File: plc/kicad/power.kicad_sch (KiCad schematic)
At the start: 81 parts, among them Q5 BSS138LT1G, Q6 CSD19537Q3, SW3 TSD003B08026A03, U14 LMR16006XDDCR, U15 TPS54560BDDAR, U16 TPS26630RGER, U17 TPS7A5201QRGRRQ1

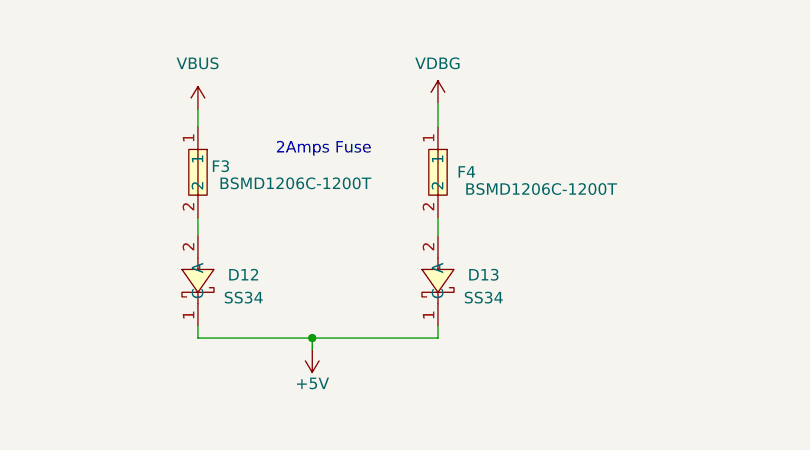
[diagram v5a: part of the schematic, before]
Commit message: Updated SMD fuses to fuse holders
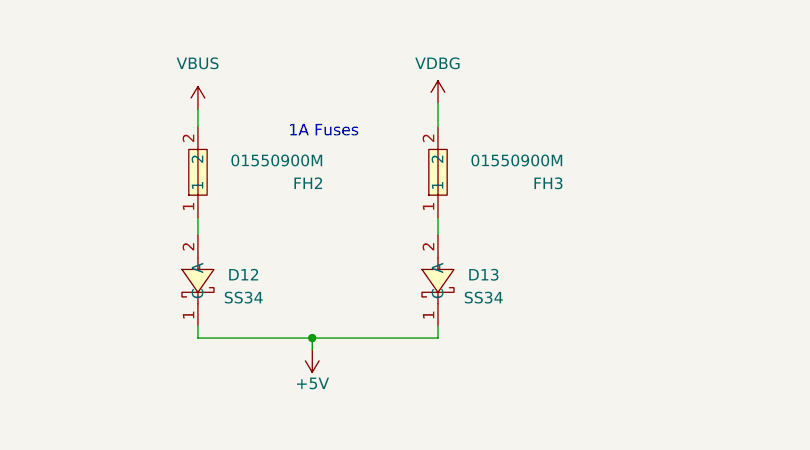
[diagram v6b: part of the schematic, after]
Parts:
- removed F3, F4: BSMD1206C-1200T, LibrePLC32:F1206, symbol LibrePLC32:BSMD1206C-1200T
- added FH2, FH3: 01550900M, LibrePLC32:FUSE-SMD_L9.8-W5.0_01550900M, symbol LibrePLC32:01550900M
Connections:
- net VBUS: now also FH2.2
- net VDBG: now also FH3.2
- net at D12.2 (A): now also FH2.1
- net at D13.2 (A): now also FH3.1
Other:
- note added: "1A Fuses"
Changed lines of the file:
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@@
 		)
 	)
-	(text "2Amps Fuse"
+	(text "1A Fuses"
 		(exclude_from_sim no)
-		(at 257.175 34.29 0)
+		(at 257.175 32.385 0)
 		(effects
 			(font
@@
 	)
 	(symbol
+		(lib_id "LibrePLC32:01550900M")
+		(at 243.205 36.83 90)
+		(unit 1)
+		(body_style 1)
+		(exclude_from_sim no)
+		(in_bom yes)
+		(on_board yes)
+		(in_pos_files yes)
+		(dnp no)
+		(property "Reference" "FH2"
+			(at 257.175 38.1 90)
+			(show_name no)
+			(do_not_autoplace no)
+			(effects
+				(font
+					(size 1.27 1.27)
+				)
+				(justify left)
+			)
+		)
+		(property "Value" "01550900M"
+			(at 257.175 35.56 90)
+			(show_name no)
+			(do_not_autoplace no)
+			(effects
+				(font
+					(size 1.27 1.27)
+				)
+				(justify left)
+			)
+		)
+		(property "Footprint" "LibrePLC32:FUSE-SMD_L9.8-W5.0_01550900M"
+			(at 250.825 36.83 0)
+			(hide yes)
+			(show_name no)
+			(do_not_autoplace no)
+			(effects
+				(font
+					(size 1.27 1.27)
+				)
+			)
+		)
+		(property "Datasheet" "https://lcsc.com/product-detail/Others_Littelfuse_01550900M_Littelfuse-01550900M_C108518.html"
+			(at 253.365 36.83 0)
+			(hide yes)
+			(show_name no)
+			(do_not_autoplace no)
+			(effects
+				(font
+					(size 1.27 1.27)
+				)
+			)
+		)
+		(property "Description" ""
+			(at 243.205 36.83 0)
+			(hide yes)
+			(show_name no)
+			(do_not_autoplace no)
+			(effects
+				(font
+					(size 1.27 1.27)
+				)
+			)
+		)
+		(property "Manufacturer" "Littelfuse(美国力特)"
+			(at 255.905 36.83 0)
+			(hide yes)
+			(show_name no)
+			(do_not_autoplace no)
+			(effects
+				(font
+					(size 1.27 1.27)
+				)
+			)
+		)
+		(property "MPN" "01550900M"
+			(at 258.445 36.83 0)
+			(hide yes)
+			(show_name no)
+			(do_not_autoplace no)
+			(effects
+				(font
+					(size 1.27 1.27)
+				)
+			)
+		)
+		(property "LCSC Part" "C108518"
+			(at 260.985 36.83 0)
+			(hide yes)
+			(show_name no)
+			(do_not_autoplace no)
+			(effects
+				(font
+					(size 1.27 1.27)
+				)
+			)
+		)
+		(pin "2"
+		)
+		(pin "1"
+		)
+		(instances
+			(project "LibrePLC32"
+				(path "/ef4c1a27-85a3-413a-9f93-a41c4f97eee5/7cb27fd0-1c73-4e87-ad2d-fb4e463ee9fb"
+					(reference "FH2")
+					(unit 1)
+				)
+			)
+		)
+	)
+	(symbol
 		(lib_id "Device:C")
 		(at 135.89 121.92 180)
@@
 	)
 	(symbol
-		(lib_id "LibrePLC32:BSMD1206C-1200T")
-		(at 243.205 36.83 270)
-		(unit 1)
-		(body_style 1)
-		(exclude_from_sim no)
-		(in_bom yes)
-		(on_board yes)
-		(in_pos_files yes)
-		(dnp no)
-		(property "Reference" "F3"
-			(at 245.745 36.195 90)
-			(show_name no)
-			(do_not_autoplace no)
-			(effects
-				(font
-					(size 1.27 1.27)
-				)
-			)
-		)
-		(property "Value" "BSMD1206C-1200T"
-			(at 254 38.1 90)
-			(show_name no)
-			(do_not_autoplace no)
-			(effects
-				(font
-					(size 1.27 1.27)
-				)
-			)
-		)
-		(property "Footprint" "LibrePLC32:F1206"
-			(at 235.585 36.83 0)
-			(hide yes)
-			(show_name no)
-			(do_not_autoplace no)
-			(effects
-				(font
-					(size 1.27 1.27)
-				)
-			)
-		)
-		(property "Datasheet" "https://www.lcsc.com/datasheet/C41367223.pdf"
-			(at 233.045 36.83 0)
-			(hide yes)
-			(show_name no)
-			(do_not_autoplace no)
-			(effects
-				(font
-					(size 1.27 1.27)
-				)
-			)
-		)
-		(property "Description" ""
-			(at 243.205 36.83 0)
-			(hide yes)
-			(show_name no)
-			(do_not_autoplace no)
-			(effects
-				(font
-					(size 1.27 1.27)
-				)
-			)
-		)
-		(property "Manufacturer" "BHFUSE(佰宏)"
-			(at 230.505 36.83 0)
-			(hide yes)
-			(show_name no)
-			(do_not_autoplace no)
-			(effects
-				(font
-					(size 1.27 1.27)
-				)
-			)
-		)
-		(property "MPN" "BSMD1206C-1200T"
-			(at 227.965 36.83 0)
-			(hide yes)
-			(show_name no)
-			(do_not_autoplace no)
-			(effects
-				(font
-					(size 1.27 1.27)
-				)
-			)
-		)
-		(property "LCSC Part" "C41367223"
-			(at 225.425 36.83 0)
-			(hide yes)
-			(show_name no)
-			(do_not_autoplace no)
-			(effects
-				(font
-					(size 1.27 1.27)
-				)
-			)
-		)
-		(pin "2"
-		)
-		(pin "1"
-		)
-		(instances
-			(project "LibrePLC32"
-				(path "/ef4c1a27-85a3-413a-9f93-a41c4f97eee5/7cb27fd0-1c73-4e87-ad2d-fb4e463ee9fb"
-					(reference "F3")
-					(unit 1)
-				)
-			)
-		)
-	)
-	(symbol
 		(lib_id "power:GND")
 		(at 54.61 143.51 0)
@@
 	)
 	(symbol
+		(lib_id "LibrePLC32:01550900M")
+		(at 269.875 36.83 90)
+		(unit 1)
+		(body_style 1)
+		(exclude_from_sim no)
+		(in_bom yes)
+		(on_board yes)
+		(in_pos_files yes)
+		(dnp no)
+		(property "Reference" "FH3"
+			(at 283.845 38.1 90)
+			(show_name no)
+			(do_not_autoplace no)
+			(effects
+				(font
+					(size 1.27 1.27)
+				)
+				(justify left)
+			)
+		)
+		(property "Value" "01550900M"
+			(at 283.845 35.56 90)
+			(show_name no)
+			(do_not_autoplace no)
+			(effects
+				(font
+					(size 1.27 1.27)
+				)
+				(justify left)
+			)
+		)
+		(property "Footprint" "LibrePLC32:FUSE-SMD_L9.8-W5.0_01550900M"
+			(at 277.495 36.83 0)
+			(hide yes)
+			(show_name no)
+			(do_not_autoplace no)
+			(effects
+				(font
+					(size 1.27 1.27)
+				)
+			)
+		)
+		(property "Datasheet" "https://lcsc.com/product-detail/Others_Littelfuse_01550900M_Littelfuse-01550900M_C108518.html"
+			(at 280.035 36.83 0)
+			(hide yes)
+			(show_name no)
+			(do_not_autoplace no)
+			(effects
+				(font
+					(size 1.27 1.27)
+				)
+			)
+		)
+		(property "Description" ""
+			(at 269.875 36.83 0)
+			(hide yes)
+			(show_name no)
+			(do_not_autoplace no)
+			(effects
+				(font
+					(size 1.27 1.27)
+				)
+			)
+		)
+		(property "Manufacturer" "Littelfuse(美国力特)"
+			(at 282.575 36.83 0)
+			(hide yes)
+			(show_name no)
+			(do_not_autoplace no)
+			(effects
+				(font
+					(size 1.27 1.27)
+				)
+			)
+		)
+		(property "MPN" "01550900M"
+			(at 285.115 36.83 0)
+			(hide yes)
+			(show_name no)
+			(do_not_autoplace no)
+			(effects
+				(font
+					(size 1.27 1.27)
+				)
+			)
+		)
+		(property "LCSC Part" "C108518"
+			(at 287.655 36.83 0)
+			(hide yes)
+			(show_name no)
+			(do_not_autoplace no)
+			(effects
+				(font
+					(size 1.27 1.27)
+				)
+			)
+		)
+		(pin "2"
+		)
+		(pin "1"
+		)
+		(instances
+			(project "LibrePLC32"
+				(path "/ef4c1a27-85a3-413a-9f93-a41c4f97eee5/7cb27fd0-1c73-4e87-ad2d-fb4e463ee9fb"
+					(reference "FH3")
+					(unit 1)
+				)
+			)
+		)
+	)
+	(symbol
 		(lib_id "Connector:TestPoint")
 		(at 347.98 99.695 180)
@@
 					(unit 1)
 				)
-			)
-		)
-	)
-	(symbol
-		(lib_id "LibrePLC32:BSMD1206C-1200T")
-		(at 269.875 36.83 270)
-		(unit 1)
-		(body_style 1)
-		(exclude_from_sim no)
-		(in_bom yes)
-		(on_board yes)
-		(in_pos_files yes)
-		(dnp no)
-		(property "Reference" "F4"
-			(at 273.05 36.83 90)
-			(show_name no)
-			(do_not_autoplace no)
-			(effects
-				(font
-					(size 1.27 1.27)
-				)
-			)
-		)
-		(property "Value" "BSMD1206C-1200T"
-			(at 281.305 38.735 90)
-			(show_name no)
-			(do_not_autoplace no)
-			(effects
-				(font
-					(size 1.27 1.27)
-				)
-			)
-		)
-		(property "Footprint" "LibrePLC32:F1206"
-			(at 262.255 36.83 0)
-			(hide yes)
-			(show_name no)
-			(do_not_autoplace no)
-			(effects
-				(font
-					(size 1.27 1.27)
-				)
-			)
-		)
-		(property "Datasheet" "https://www.lcsc.com/datasheet/C41367223.pdf"
-			(at 259.715 36.83 0)
-			(hide yes)
-			(show_name no)
-			(do_not_autoplace no)
-			(effects
-				(font
-					(size 1.27 1.27)
-				)
-			)
-		)
-		(property "Description" ""
-			(at 269.875 36.83 0)
-			(hide yes)
-			(show_name no)
-			(do_not_autoplace no)
-			(effects
-				(font
-					(size 1.27 1.27)
-				)
-			)
-		)
-		(property "Manufacturer" "BHFUSE(佰宏)"
-			(at 257.175 36.83 0)
-			(hide yes)
-			(show_name no)
-			(do_not_autoplace no)
-			(effects
-				(font
-					(size 1.27 1.27)
-				)
-			)
-		)
-		(property "MPN" "BSMD1206C-1200T"
-			(at 254.635 36.83 0)
-			(hide yes)
-			(show_name no)
-			(do_not_autoplace no)
-			(effects
-				(font
-					(size 1.27 1.27)
-				)
-			)
-		)
-		(property "LCSC Part" "C41367223"
-			(at 252.095 36.83 0)
-			(hide yes)
-			(show_name no)
-			(do_not_autoplace no)
-			(effects
-				(font
-					(size 1.27 1.27)
-				)
-			)
-		)
-		(pin "2"
-		)
-		(pin "1"
-		)
-		(instances
-			(project "LibrePLC32"
-				(path "/ef4c1a27-85a3-413a-9f93-a41c4f97eee5/7cb27fd0-1c73-4e87-ad2d-fb4e463ee9fb"
-					(reference "F4")
-					(unit 1)
-				)

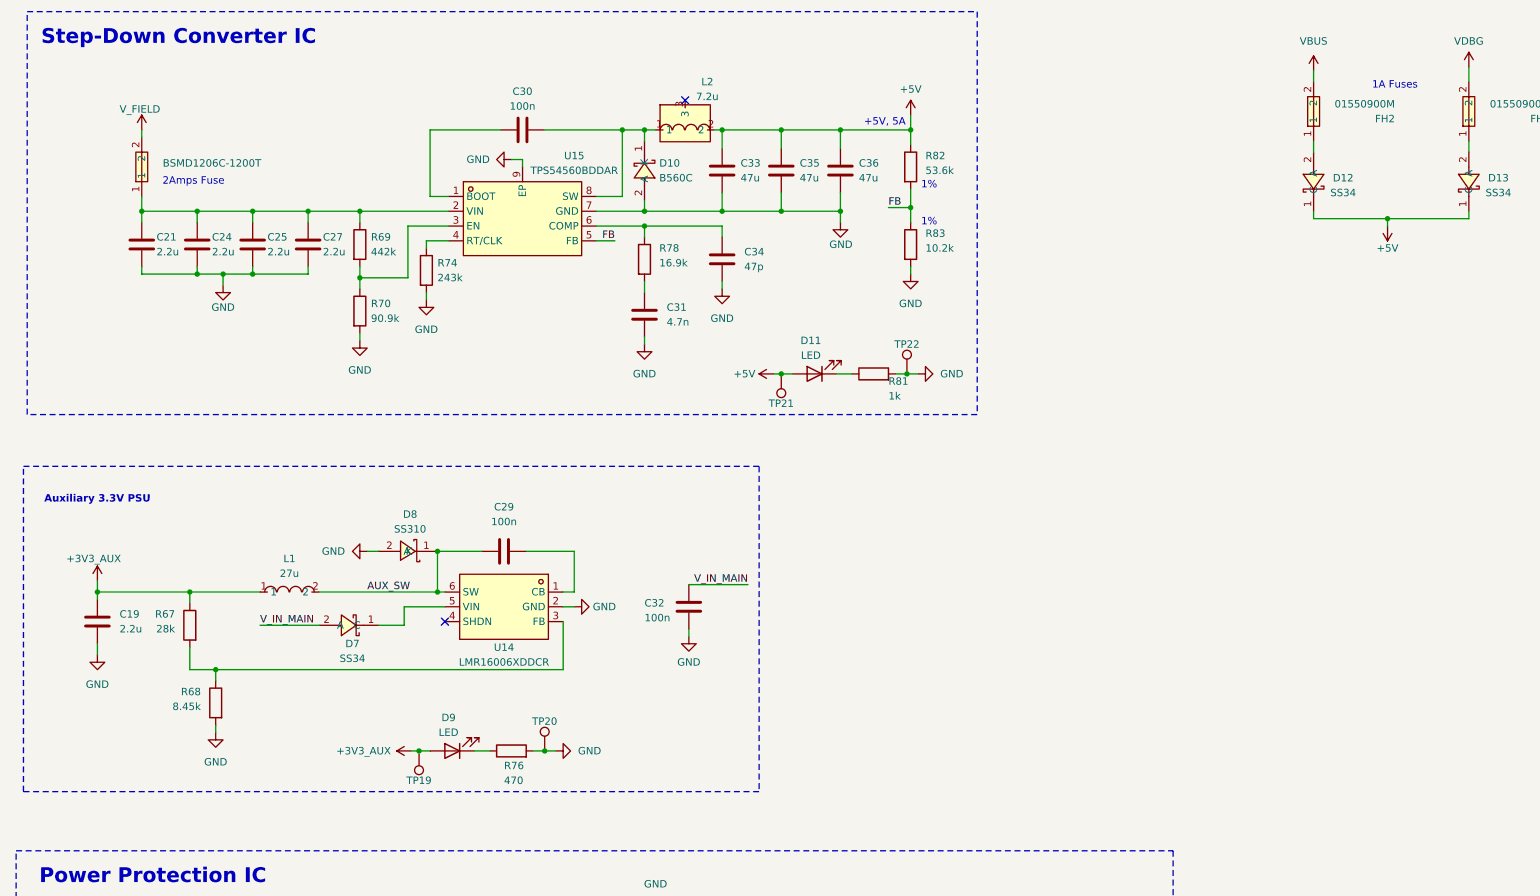
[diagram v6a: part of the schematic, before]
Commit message: Modified 3V3 aux to zener
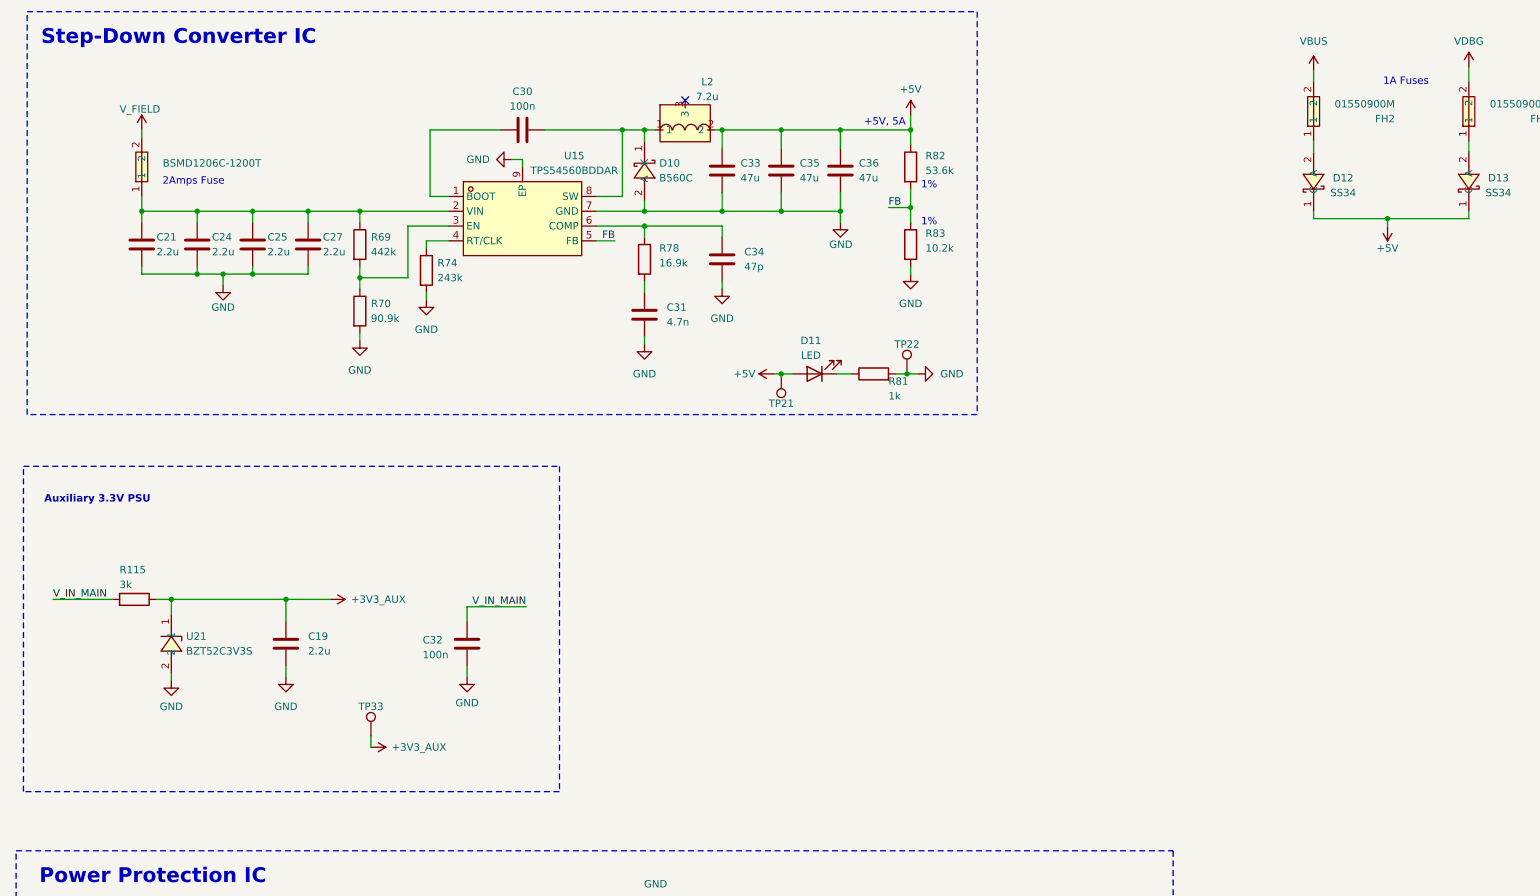
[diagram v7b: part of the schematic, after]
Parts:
- removed C29: 100n, Capacitor_SMD:C_0603_1608Metric, symbol Device:C
- removed D7: SS34, LibrePLC32:SMA_L4.3-W2.7-LS5.1-RD, symbol LibrePLC32:SS34_C908680
- removed D8: SS310, LibrePLC32:SMB_L4.6-W3.6-LS5.3-RD, symbol LibrePLC32:SS310_C14281
- removed D9: LED, LED_SMD:LED_0805_2012Metric, symbol Device:LED
- removed L1: 27u, LibrePLC32:IND-SMD_L3.5-W3.0_SLF0302, symbol LibrePLC32:ASPI-0315S-270M-T
- removed R67: 28k, Resistor_SMD:R_0603_1608Metric, symbol Device:R
- removed R68: 8.45k, Resistor_SMD:R_0603_1608Metric, symbol Device:R
- removed R76: 470, Resistor_SMD:R_0603_1608Metric, symbol Device:R
- removed TP19, TP20: TestPoint, TestPoint:TestPoint_Pad_D3.0mm, symbol Connector:TestPoint
- removed U14: LMR16006XDDCR, LibrePLC32:SOT-23-6_L2.9-W1.6-P0.95-LS2.8-BR, symbol LibrePLC32:LMR16006XDDCR
- added R115: 3k, Resistor_SMD:R_2512_6332Metric, symbol Device:R
- added TP33: TestPoint, TestPoint:TestPoint_Pad_D4.0mm, symbol Connector:TestPoint
- added U21: BZT52C3V3S, LibrePLC32:SOD-323_L1.7-W1.3-LS2.5-RD-1, symbol LibrePLC32:BZT52C3V3S_C5270765
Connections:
- net +3V3_AUX: now also R115.1, TP33.1, U21.1
- net GND: now also U21.2
- net V_IN_MAIN: now also R115.2
- no-connect marks 16 -> 15
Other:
- moved on the sheet: C32

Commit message: Slight silkscreen & component adjustment
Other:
- moved on the sheet: C38, C39, C40, C41, D14, R86, R87, R88, R89, TP23, TP24, U17
